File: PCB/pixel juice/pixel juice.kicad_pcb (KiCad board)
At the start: 4 copper layers, 99.7 x 52.7 mm, 18 parts, among them J1 n8 Bus Connector, J2 IRQ_SEL, J3 AUDIO_CLK, J4 PJRAN3X1U03X, J5 TO_AMP, J6 FROM_AMP, U1 TMS9128, U2 TMS4416, U3 TMS4416, U4 74LS32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

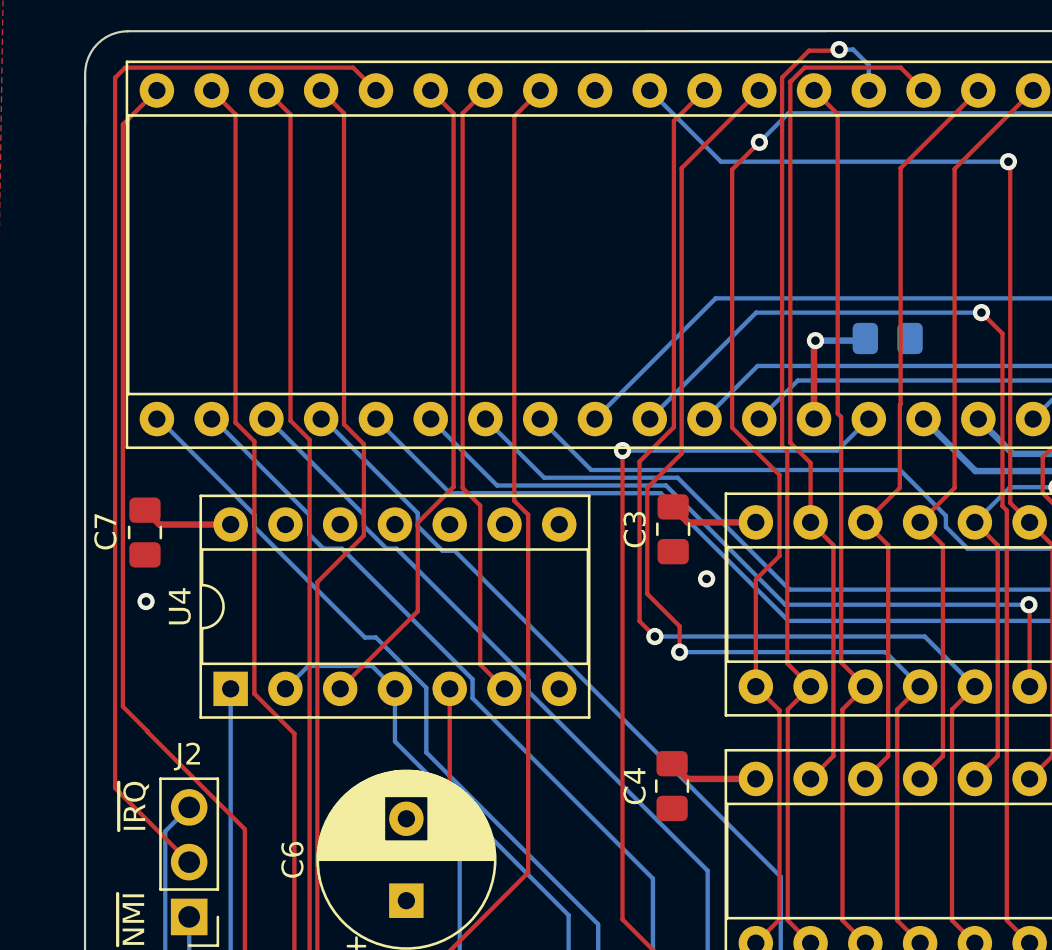
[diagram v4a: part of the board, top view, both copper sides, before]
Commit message: added 2 new soundcard designs
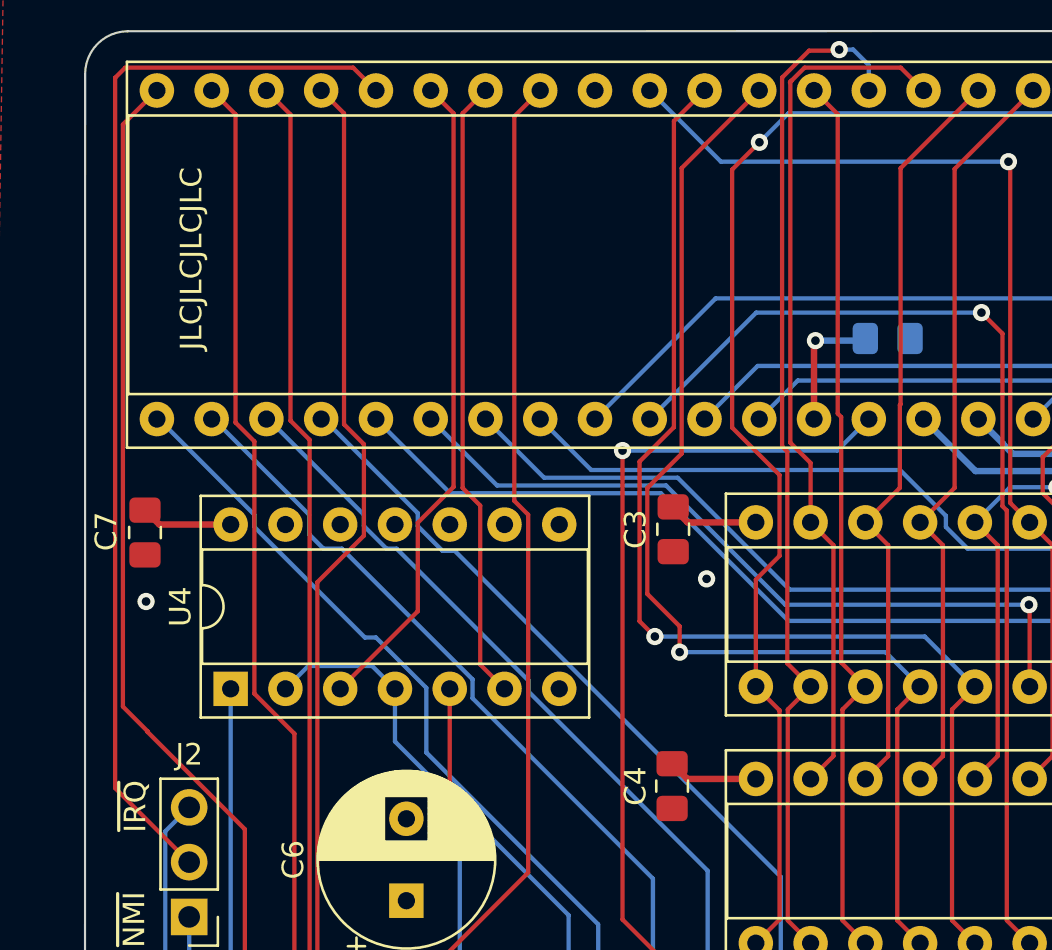
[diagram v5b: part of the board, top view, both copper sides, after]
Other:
- board text added: "JLCJLCJLCJLC"
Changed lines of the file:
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@@
       (outputformat 1)
       (mirror false)
-      (drillshape 1)
+      (drillshape 0)
       (scaleselection 1)
-      (outputdirectory "")
+      (outputdirectory "gerbers/")
     )
   )
@@
     (fp_line (start 1 0.625) (end -1 0.625) (layer "F.Fab") (width 0.1))
     (fp_line (start -1 0.625) (end -1 -0.625) (layer "F.Fab") (width 0.1))
-    (pad "1" smd roundrect (at -1.0375 0 270) (size 1.175 1.45) (layers "F.Cu" "F.Paste" "F.Mask") (roundrect_rratio 0.212766)
+    (pad "1" smd roundrect (at -1.0375 0 270) (size 1.175 1.45) (layers "F.Cu" "F.Paste" "F.Mask") (roundrect_rratio 0.2127659574)
       (net 1 "+5V") (pintype "passive"))
-    (pad "2" smd roundrect (at 1.0375 0 270) (size 1.175 1.45) (layers "F.Cu" "F.Paste" "F.Mask") (roundrect_rratio 0.212766)
+    (pad "2" smd roundrect (at 1.0375 0 270) (size 1.175 1.45) (layers "F.Cu" "F.Paste" "F.Mask") (roundrect_rratio 0.2127659574)
       (net 2 "GND") (pintype "passive"))
     (model "${KICAD6_3DMODEL_DIR}/Capacitor_SMD.3dshapes/C_0805_2012Metric.wrl"
@@
     (fp_line (start -1 -0.625) (end 1 -0.625) (layer "F.Fab") (width 0.1))
     (fp_line (start -1 0.625) (end -1 -0.625) (layer "F.Fab") (width 0.1))
-    (pad "1" smd roundrect (at -1.0375 0 270) (size 1.175 1.45) (layers "F.Cu" "F.Paste" "F.Mask") (roundrect_rratio 0.212766)
+    (pad "1" smd roundrect (at -1.0375 0 270) (size 1.175 1.45) (layers "F.Cu" "F.Paste" "F.Mask") (roundrect_rratio 0.2127659574)
       (net 1 "+5V") (pintype "passive"))
-    (pad "2" smd roundrect (at 1.0375 0 270) (size 1.175 1.45) (layers "F.Cu" "F.Paste" "F.Mask") (roundrect_rratio 0.212766)
+    (pad "2" smd roundrect (at 1.0375 0 270) (size 1.175 1.45) (layers "F.Cu" "F.Paste" "F.Mask") (roundrect_rratio 0.2127659574)
       (net 2 "GND") (pintype "passive"))
     (model "${KICAD6_3DMODEL_DIR}/Capacitor_SMD.3dshapes/C_0805_2012Metric.wrl"
@@
     (fp_line (start -1 0.625) (end -1 -0.625) (layer "F.Fab") (width 0.1))
     (fp_line (start 1 -0.625) (end 1 0.625) (layer "F.Fab") (width 0.1))
-    (pad "1" smd roundrect (at -1.0375 0 270) (size 1.175 1.45) (layers "F.Cu" "F.Paste" "F.Mask") (roundrect_rratio 0.212766)
+    (pad "1" smd roundrect (at -1.0375 0 270) (size 1.175 1.45) (layers "F.Cu" "F.Paste" "F.Mask") (roundrect_rratio 0.2127659574)
       (net 1 "+5V") (pintype "passive"))
-    (pad "2" smd roundrect (at 1.0375 0 270) (size 1.175 1.45) (layers "F.Cu" "F.Paste" "F.Mask") (roundrect_rratio 0.212766)
+    (pad "2" smd roundrect (at 1.0375 0 270) (size 1.175 1.45) (layers "F.Cu" "F.Paste" "F.Mask") (roundrect_rratio 0.2127659574)
       (net 2 "GND") (pintype "passive"))
     (model "${KICAD6_3DMODEL_DIR}/Capacitor_SMD.3dshapes/C_0805_2012Metric.wrl"
@@
     (fp_line (start -1 -0.625) (end -1 0.625) (layer "B.Fab") (width 0.1))
     (fp_line (start 1 0.625) (end 1 -0.625) (layer "B.Fab") (width 0.1))
-    (pad "1" smd roundrect (at -1.0375 0) (size 1.175 1.45) (layers "B.Cu" "B.Paste" "B.Mask") (roundrect_rratio 0.212766)
+    (pad "1" smd roundrect (at -1.0375 0) (size 1.175 1.45) (layers "B.Cu" "B.Paste" "B.Mask") (roundrect_rratio 0.2127659574)
       (net 1 "+5V") (pintype "passive"))
-    (pad "2" smd roundrect (at 1.0375 0) (size 1.175 1.45) (layers "B.Cu" "B.Paste" "B.Mask") (roundrect_rratio 0.212766)
+    (pad "2" smd roundrect (at 1.0375 0) (size 1.175 1.45) (layers "B.Cu" "B.Paste" "B.Mask") (roundrect_rratio 0.2127659574)
       (net 2 "GND") (pintype "passive"))
     (model "${KICAD6_3DMODEL_DIR}/Capacitor_SMD.3dshapes/C_0805_2012Metric.wrl"
@@
     (effects (font (size 1 1) (thickness 0.15)))
   )
+  (gr_text "JLCJLCJLCJLC" (at 105.5 75.85 90) (layer "F.SilkS")
+    (effects (font (size 1 1) (thickness 0.2)))
+  )
   (gr_text "+5V" (at 166.25 87.05) (layer "F.SilkS")
     (effects (font (size 1 1) (thickness 0.15)))
@@
   )
   (dimension (type aligned) (layer "Cmts.User")
-    (pts (xy 176.25 114.45) (xy 176.25 116.85))
+    (pts (xy 176.25 114.425) (xy 176.25 116.9))
     (height -10.7)
-    (gr_text "2.4000 mm" (at 185.8 115.65 90) (layer "Cmts.User")
-      (effects (font (size 1 1) (thickness 0.15)))
-    )
+    (gr_text "2.4750 mm" (at 185.8 115.6625 90) (layer "Cmts.User")
+      (effects (font (size 1 1) (thickness 0.15)))
+    )
